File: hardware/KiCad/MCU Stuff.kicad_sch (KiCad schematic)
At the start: 35 parts, among them U1 STM32F072RBT6, U8 XL7005A, U9 XL7005A

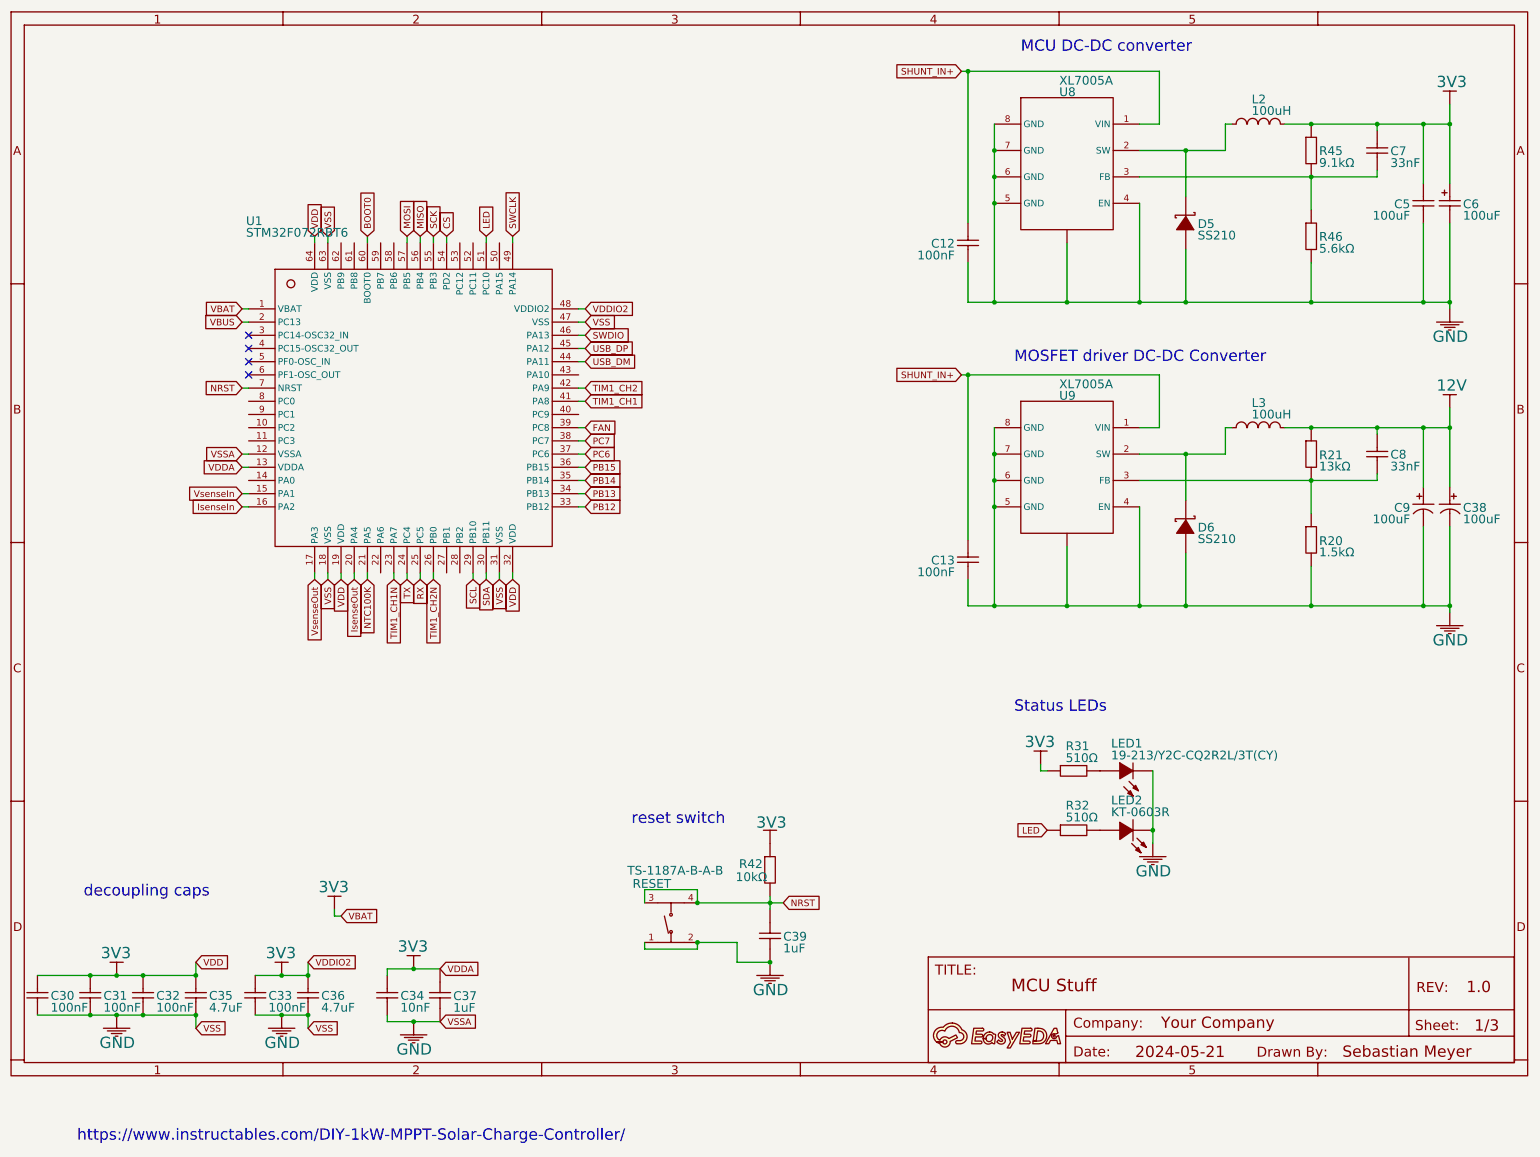
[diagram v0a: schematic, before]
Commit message: added the new 10v regulator
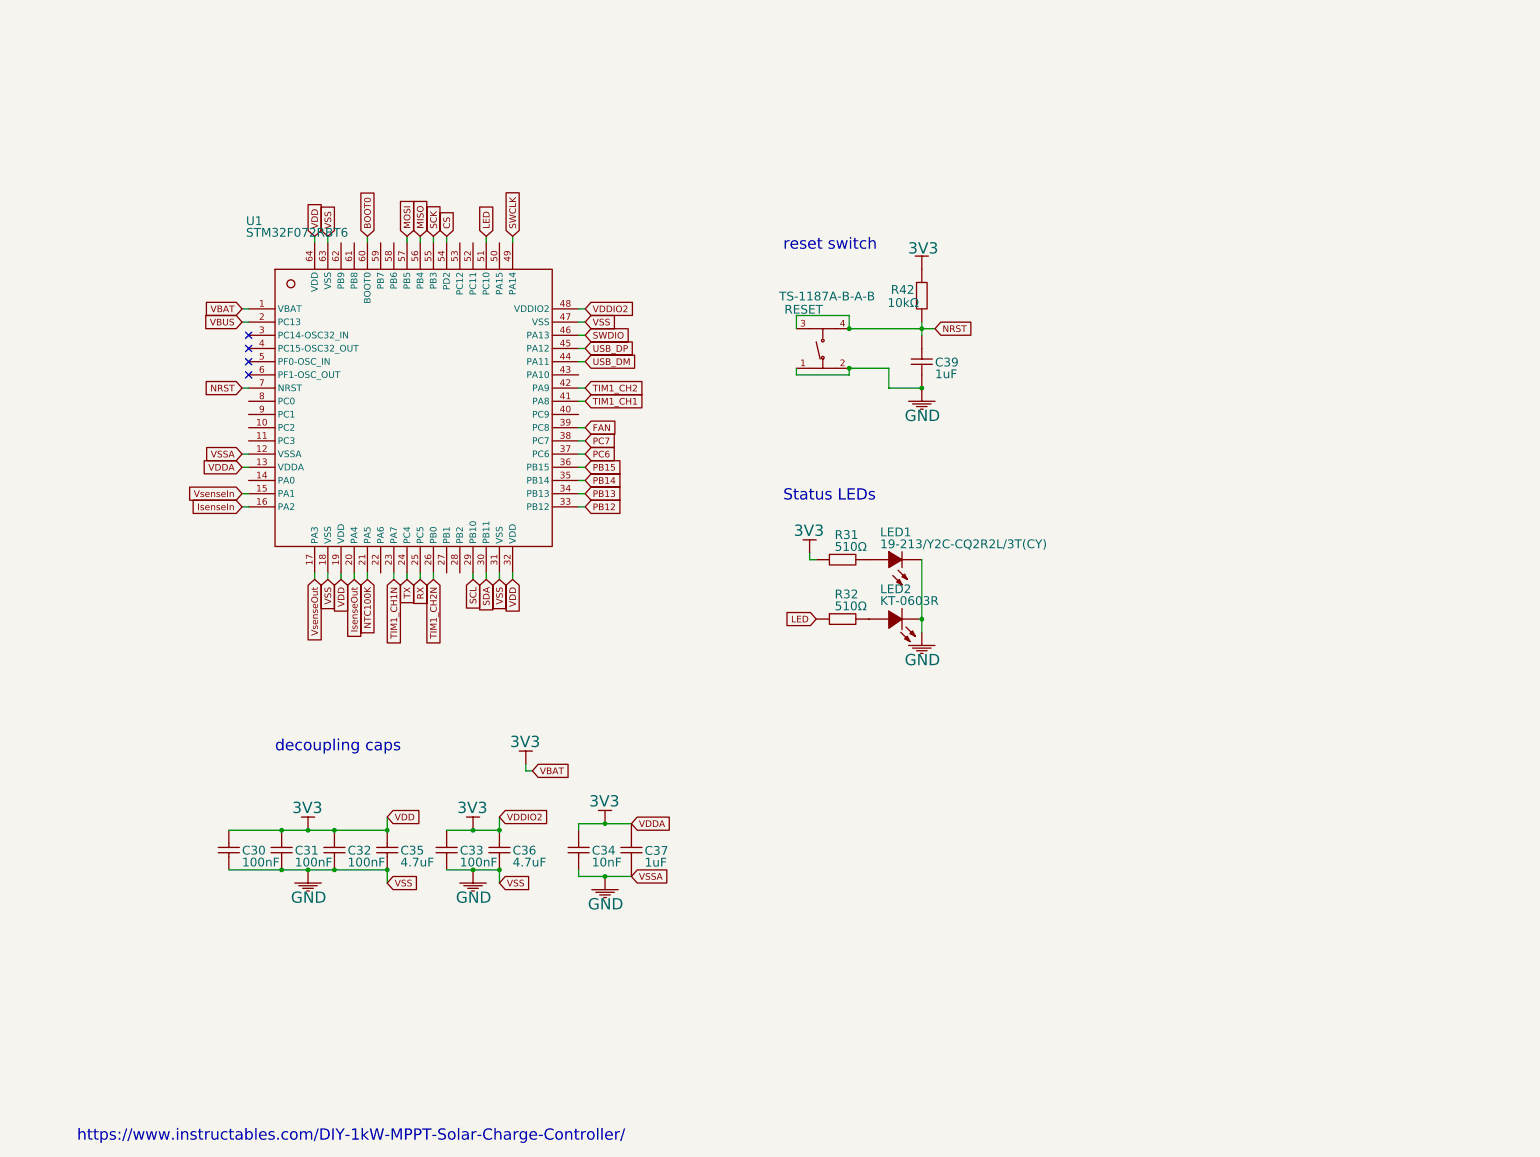
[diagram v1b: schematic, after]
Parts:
- removed A: A, symbol Unknown_0_-806
- removed C12: 100nF, symbol CL21B104KCFNNNE
- removed C13: 100nF, symbol CL21B104KCFNNNE_1
- removed C38: 100uF, symbol RVE1C101M0605-C88658_1
- removed C5: 100uF, symbol CL31A107MQHNNNE
- removed C6: 100uF, symbol TAJB107K006RNJ
- removed C7: 33nF, symbol CL10B333KB8NNNC
- removed C8: 33nF, symbol CL10B333KB8NNNC_1
- removed C9: 100uF, symbol RVE1C101M0605-C88658
- removed D5: SS210, symbol SS210
- removed D6: SS210, symbol SS210_1
- removed L2: 100uH, symbol YNR6028-101M
- removed L3: 100uH, symbol YNR6028-101M_1
- removed R20: 1.5kΩ, symbol 0603WAF1501T5E
- removed R21: 13kΩ, symbol 0603WAF1302T5E
- removed R45: 9.1kΩ, symbol 0603WAF9101T5E
- removed R46: 5.6kΩ, symbol 0603WAF5601T5E
- removed U8: XL7005A, symbol XL7005A
- removed U9: XL7005A, symbol XL7005A_1
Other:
- note removed: "MCU DC-DC converter"
- note removed: "MOSFET driver DC-DC Converter"
- moved on the sheet: C30, C31, C32, C33, C34, C35, C36, C37, C39, LED1, LED2, R31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
